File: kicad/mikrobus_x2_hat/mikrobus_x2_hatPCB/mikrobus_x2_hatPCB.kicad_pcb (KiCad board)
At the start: 2 copper layers, 65 x 56.5 mm, 9 parts, among them IC1 MIKROE-924, IC2 MIKROE-924, J1 RPi_GPIO

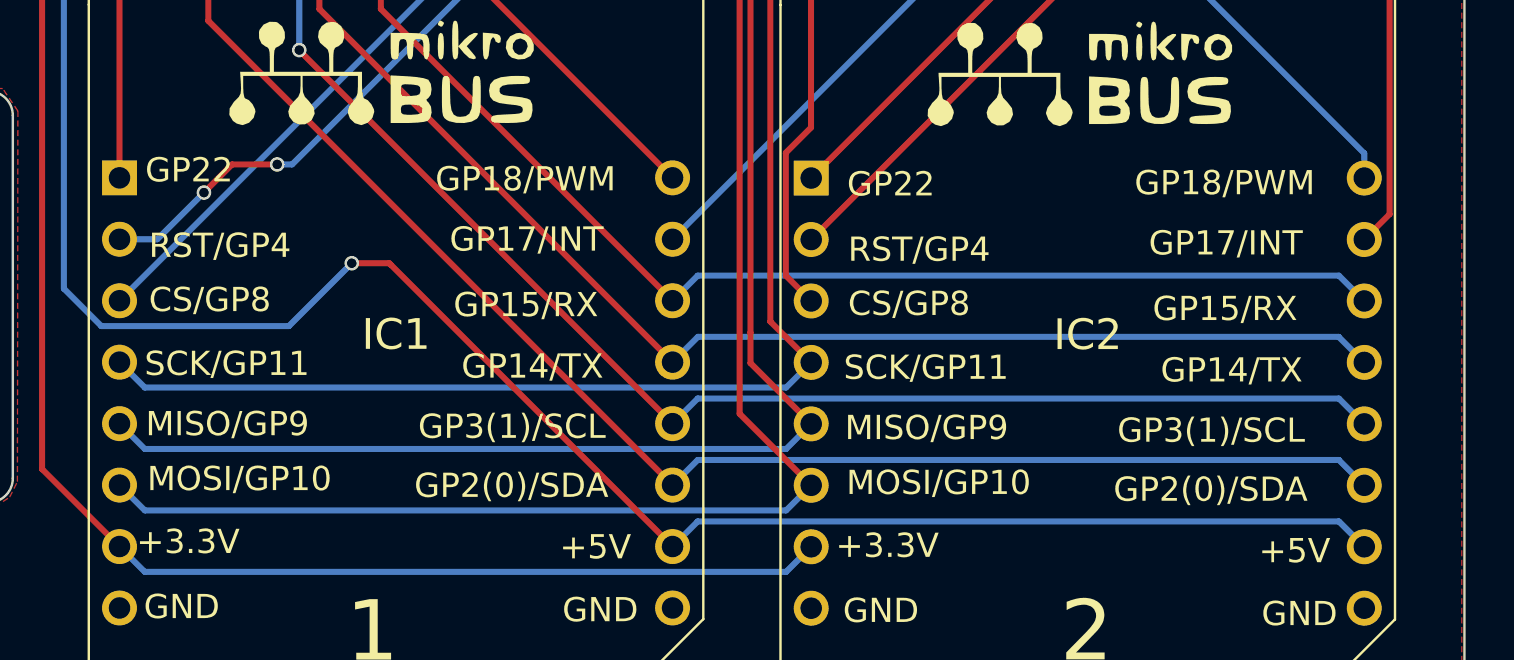
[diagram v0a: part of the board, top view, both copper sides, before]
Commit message: fix serigraphy
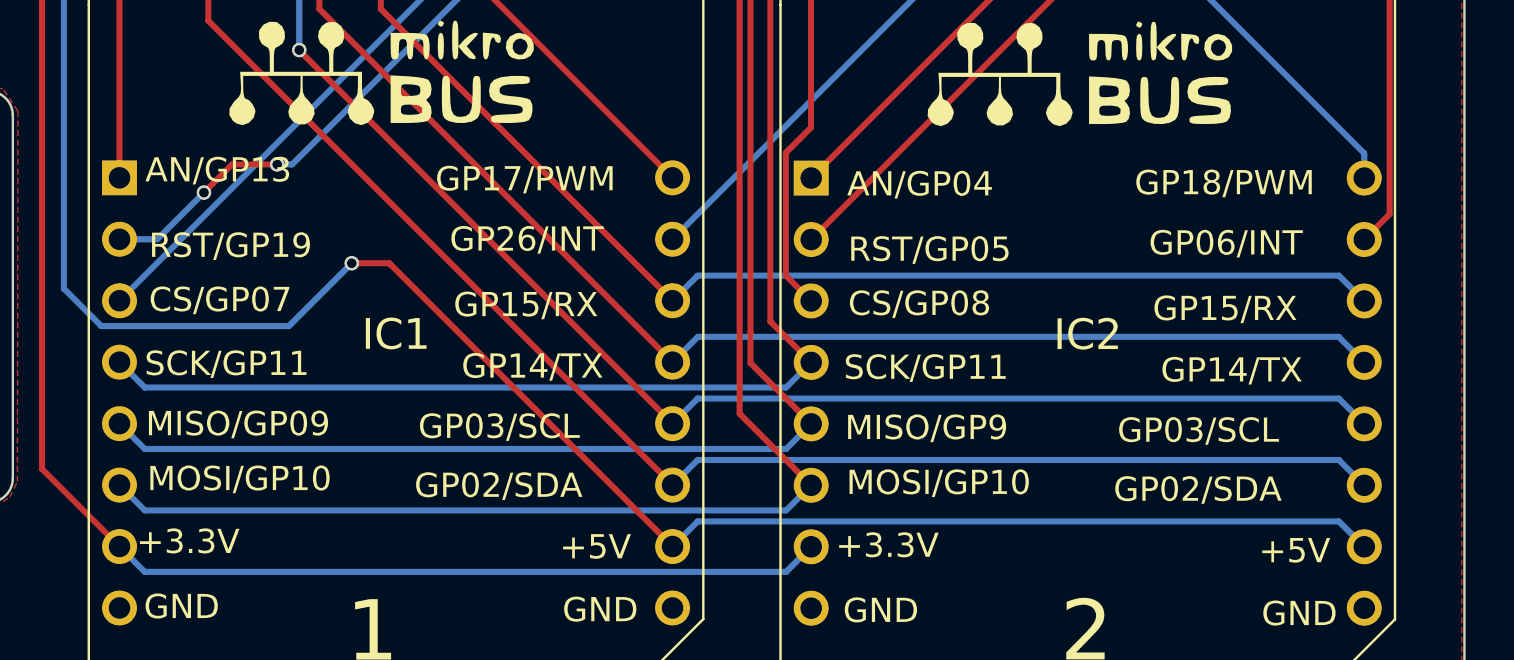
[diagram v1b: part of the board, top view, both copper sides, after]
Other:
- board text added: "AN/GP04"
- board text added: "AN/GP13"
- board text added: "CS/GP07"
- board text added: "CS/GP08"
- board text added: "GP02/SDA"
- board text added: "GP03/SCL"
- board text added: "GP06/INT"
- board text added: "GP17/PWM"
- board text added: "GP26/INT"
- board text added: "MISO/GP09"
- board text added: "RST/GP05"
- board text added: "RST/GP19"
- board text removed: "CS/GP8"
- board text removed: "GP17/INT"
- board text removed: "GP2(0)/SDA"
- board text removed: "GP22"
- board text removed: "GP3(1)/SCL"
- board text removed: "RST/GP4"
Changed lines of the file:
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@@
 	)
 	(paper "A4")
+	(title_block
+		(title "Mikrobus Pi Hat x2")
+		(date "2024-09-03")
+		(rev "v1.1")
+	)
 	(layers
 		(0 "F.Cu" signal)
@@
 				(font
 					(size 1.27 1.27)
+					(thickness 0.15)
 				)
 			)
@@
 				(font
 					(size 1.27 1.27)
+					(thickness 0.15)
 				)
 			)
@@
 				(font
 					(size 1.27 1.27)
+					(thickness 0.15)
 				)
 			)
@@
 				(font
 					(size 1.27 1.27)
+					(thickness 0.15)
 				)
 			)
@@
 				(font
 					(size 1.27 1.27)
+					(thickness 0.15)
 				)
 			)
@@
 				(font
 					(size 1.27 1.27)
+					(thickness 0.15)
 				)
 			)
@@
 				(font
 					(size 1.27 1.27)
+					(thickness 0.15)
 				)
 			)
@@
 				(font
 					(size 1.27 1.27)
+					(thickness 0.15)
 				)
 			)
@@
 				(font
 					(size 1.27 1.27)
+					(thickness 0.15)
 				)
 			)
@@
 				(font
 					(size 1.27 1.27)
+					(thickness 0.15)
 				)
 			)
@@
 				(font
 					(size 1.27 1.27)
+					(thickness 0.15)
 				)
 			)
@@
 				(font
 					(size 1.27 1.27)
+					(thickness 0.15)
 				)
 			)
@@
 				(font
 					(size 1.27 1.27)
+					(thickness 0.15)
 				)
 			)
@@
 				(font
 					(size 1.27 1.27)
+					(thickness 0.15)
 				)
 			)
@@
 				(font
 					(size 1.27 1.27)
+					(thickness 0.15)
 				)
 			)
@@
 				(font
 					(size 1.27 1.27)
+					(thickness 0.15)
 				)
 			)
@@
 				(font
 					(size 1.27 1.27)
+					(thickness 0.15)
 				)
 			)
@@
 				(font
 					(size 1.27 1.27)
+					(thickness 0.15)
 				)
 			)
@@
 				(font
 					(size 1.27 1.27)
+					(thickness 0.15)
 				)
 			)
@@
 				(font
 					(size 1.27 1.27)
+					(thickness 0.15)
 				)
 			)
@@
 				(font
 					(size 1.27 1.27)
+					(thickness 0.15)
 				)
 			)
@@
 				(font
 					(size 1.27 1.27)
+					(thickness 0.15)
 				)
 			)
@@
 				(font
 					(size 1.27 1.27)
+					(thickness 0.15)
 				)
 			)
@@
 				(font
 					(size 1.27 1.27)
+					(thickness 0.15)
 				)
 			)
@@
 				(font
 					(size 1.27 1.27)
+					(thickness 0.15)
 				)
 			)
@@
 				(font
 					(size 1.27 1.27)
+					(thickness 0.15)
 				)
 			)
@@
 				(font
 					(size 1.27 1.27)
+					(thickness 0.15)
 				)
 			)
@@
 		(layer "Edge.Cuts")
 	)
-	(gr_text "CS/GP8"
+	(gr_text "CS/GP07"
 		(at 125.79 99.74 0)
 		(layer "F.SilkS")
@@
 		)
 	)
-	(gr_text "GP22"
+	(gr_text "AN/GP04"
 		(at 154.65 94.96 0)
 		(layer "F.SilkS")
@@
 		)
 	)
-	(gr_text "GP3(1)/SCL"
+	(gr_text "GP03/SCL"
 		(at 165.82 105.14 0)
 		(layer "F.SilkS")
@@
 		)
 	)
-	(gr_text "GP17/INT"
+	(gr_text "GP26/INT"
 		(at 138.22 97.24 0)
 		(layer "F.SilkS")
@@
 		)
 	)
-	(gr_text "GP18/PWM"
+	(gr_text "GP17/PWM"
 		(at 137.63 94.75 0)
 		(layer "F.SilkS")
@@
 		)
 	)
-	(gr_text "CS/GP8"
+	(gr_text "CS/GP08"
 		(at 154.69 99.9 0)
 		(layer "F.SilkS")
@@
 		)
 	)
-	(gr_text "GP17/INT"
+	(gr_text "GP06/INT"
 		(at 167.12 97.4 0)
 		(layer "F.SilkS")
@@
 		)
 	)
-	(gr_text "RST/GP4"
+	(gr_text "RST/GP19"
 		(at 125.79 97.5 0)
 		(layer "F.SilkS")
@@
 		)
 	)
-	(gr_text "GP3(1)/SCL"
+	(gr_text "GP03/SCL"
 		(at 136.92 104.98 0)
 		(layer "F.SilkS")
@@
 		)
 	)
-	(gr_text "MISO/GP9"
+	(gr_text "MISO/GP09"
 		(at 125.66 104.87 0)
 		(layer "F.SilkS")
@@
 		)
 	)
-	(gr_text "GP2(0)/SDA"
+	(gr_text "GP02/SDA"
 		(at 165.66 107.58 0)
 		(layer "F.SilkS")
@@
 		)
 	)
-	(gr_text "GP22"
+	(gr_text "AN/GP13"
 		(at 125.64 94.38 0)
 		(layer "F.SilkS")
@@
 		)
 	)
-	(gr_text "GP2(0)/SDA"
+	(gr_text "GP02/SDA"
 		(at 136.76 107.42 0)
 		(layer "F.SilkS")
@@
 		)
 	)
-	(gr_text "RST/GP4"
+	(gr_text "RST/GP05"
 		(at 154.69 97.66 0)
 		(layer "F.SilkS")

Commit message: debut routage
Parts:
- added JP1: Jumper_3_Bridged12, Connector_PinSocket_2.54mm:PinSocket_1x03_P2.54mm_Vertical, F.Cu at (147.5, 123.6)
- added JP2: Jumper_3_Bridged12, Connector_PinSocket_2.54mm:PinSocket_1x03_P2.54mm_Vertical, F.Cu at (147.5, 119.0)
- J1: footprint RPi_Hat:Samtec_HLE-120-02-XXX-DV-BE-XX-XX -> Connector_PinSocket_2.54mm:PinSocket_2x20_P2.54mm_Vertical; moved to B.Cu
- moved J1 24.2 mm to (123.5, 75.9), turned to -90 degrees
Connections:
- net Net-(IC1-AN) renamed /AN1
- net Net-(IC1-CS) renamed /CS1
- net Net-(IC1-INT) renamed /INT1
- net Net-(IC1-MISO) renamed /MISO
- net Net-(IC1-MOSI) renamed /MOSI
- net Net-(IC1-PWM) renamed /PWM1
- net Net-(IC1-RST) renamed /RST1
- net Net-(IC1-SCK) renamed /SCLK
- net Net-(IC1-SCL) renamed /SCL
- net Net-(IC1-SDA) renamed /SDA
- net Net-(IC2-AN) renamed /AN2
- net Net-(IC2-CS) renamed /CS2
- net Net-(IC2-INT) renamed /INT2
- net Net-(IC2-PWM) renamed /PWM2
- net Net-(IC2-RST) renamed /RST2
- IC1 pad 11: Net-(IC1-RX) -> /TX1
- IC1 pad 12: Net-(IC1-TX) -> /RX1
- IC2 pad 11: Net-(IC1-RX) -> /TX2
- IC2 pad 12: Net-(IC1-TX) -> /RX2
- J1 pad 10: Net-(IC1-RX) -> Net-(J1-BCM15_RXD)
- J1 pad 8: Net-(IC1-TX) -> Net-(J1-BCM14_TXD)
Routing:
- net (no net): track 0.00 -> 128.6 mm
- net Net-(IC1-TX): track 66.1 -> 0.00 mm
- net Net-(J1-BCM14_TXD): track 0.00 -> 64.9 mm
- net Net-(IC1-RX): track 62.5 -> 0.00 mm
- net Net-(J1-BCM15_RXD): track 0.00 -> 53.1 mm
- net /TX2: track 0.00 -> 44.0 mm
- net /RX2: track 0.00 -> 30.6 mm
- net /PWM2: track 53.3 -> 47.9 mm, vias 3 -> 0
- net /CS1: track 39.9 -> 43.2 mm
- net /RST1: vias 3 -> 1
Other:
- board text added: "CS/GP8"
- board text added: "GP17/INT"
- board text added: "GP2(0)/SDA"
- board text added: "GP22"
- board text added: "GP3(1)/SCL"
- board text added: "RST/GP4"
- board text removed: "AN/GP04"
- board text removed: "AN/GP13"
- board text removed: "CS/GP07"
- board text removed: "CS/GP08"
- board text removed: "GP02/SDA"
- board text removed: "GP03/SCL"
- board text removed: "GP06/INT"
- board text removed: "GP17/PWM"
- board text removed: "GP26/INT"
- board text removed: "MISO/GP09"
- board text removed: "RST/GP05"
- board text removed: "RST/GP19"

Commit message: final commit
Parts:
- added ?: LOGO, footprint:logo_csug, B.Cu at (169.1, 84.4)
- G*** (x2): footprint logo:mikro_logo -> footprint:mikro_logo
- IC1, IC2: footprint MIKROE-924:MIKROE924 -> footprint:MIKROE924
- JP1, JP2: footprint Connector_PinSocket_2.54mm:PinSocket_1x03_P2.54mm_Vertical -> Connector_PinHeader_2.54mm:PinHeader_1x03_P2.54mm_Vertical
- moved JP2 1.59 mm to (147.4, 120.6)
- moved JP1 0.82 mm to (147.4, 124.5)
- moved J1 0.13 mm to (123.7, 75.8)
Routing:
- net (no net): track 128.6 -> 58.9 mm
- net /TX1: track 0.00 -> 32.8 mm
- net /RX1: track 0.00 -> 19.8 mm
- net /PWM2: track 47.9 -> 54.0 mm
- net 5V: track 92.9 -> 89.8 mm
- net /CS1: track 43.2 -> 41.3 mm
- net Net-(J1-BCM15_RXD): track 53.1 -> 54.7 mm
- net /SCLK: track 54.6 -> 56.1 mm
- net /RST2: track 25.0 -> 26.5 mm
- net /INT1: track 25.3 -> 26.7 mm
- net /AN1: track 19.6 -> 21.0 mm
- net /AN2: track 21.4 -> 22.9 mm
- net /RST1: track 42.6 -> 44.0 mm
- net /PWM1: track 26.9 -> 25.6 mm
- net /MISO: track 58.2 -> 59.6 mm
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- added copper zone on B.Cu, net GND
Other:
- board text added: "LSI Carnot Persyval Lab LIG Slices FR"
- board text added: "Mikro 1"
- board text added: "Mikro 2"
- board text added: "S/N"
- board text added: "UART sel."
